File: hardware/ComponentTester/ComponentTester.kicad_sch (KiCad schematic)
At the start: 18 parts, among them J1 Conn_01x06_Socket, J2 AVR-ISP-6, J3 Conn_02x07_Counter_Clockwise, J4 GameBoy_GamePak_DMG-09, SW1 SW_Push, U1 ATmega328P-A, X1 16MHz

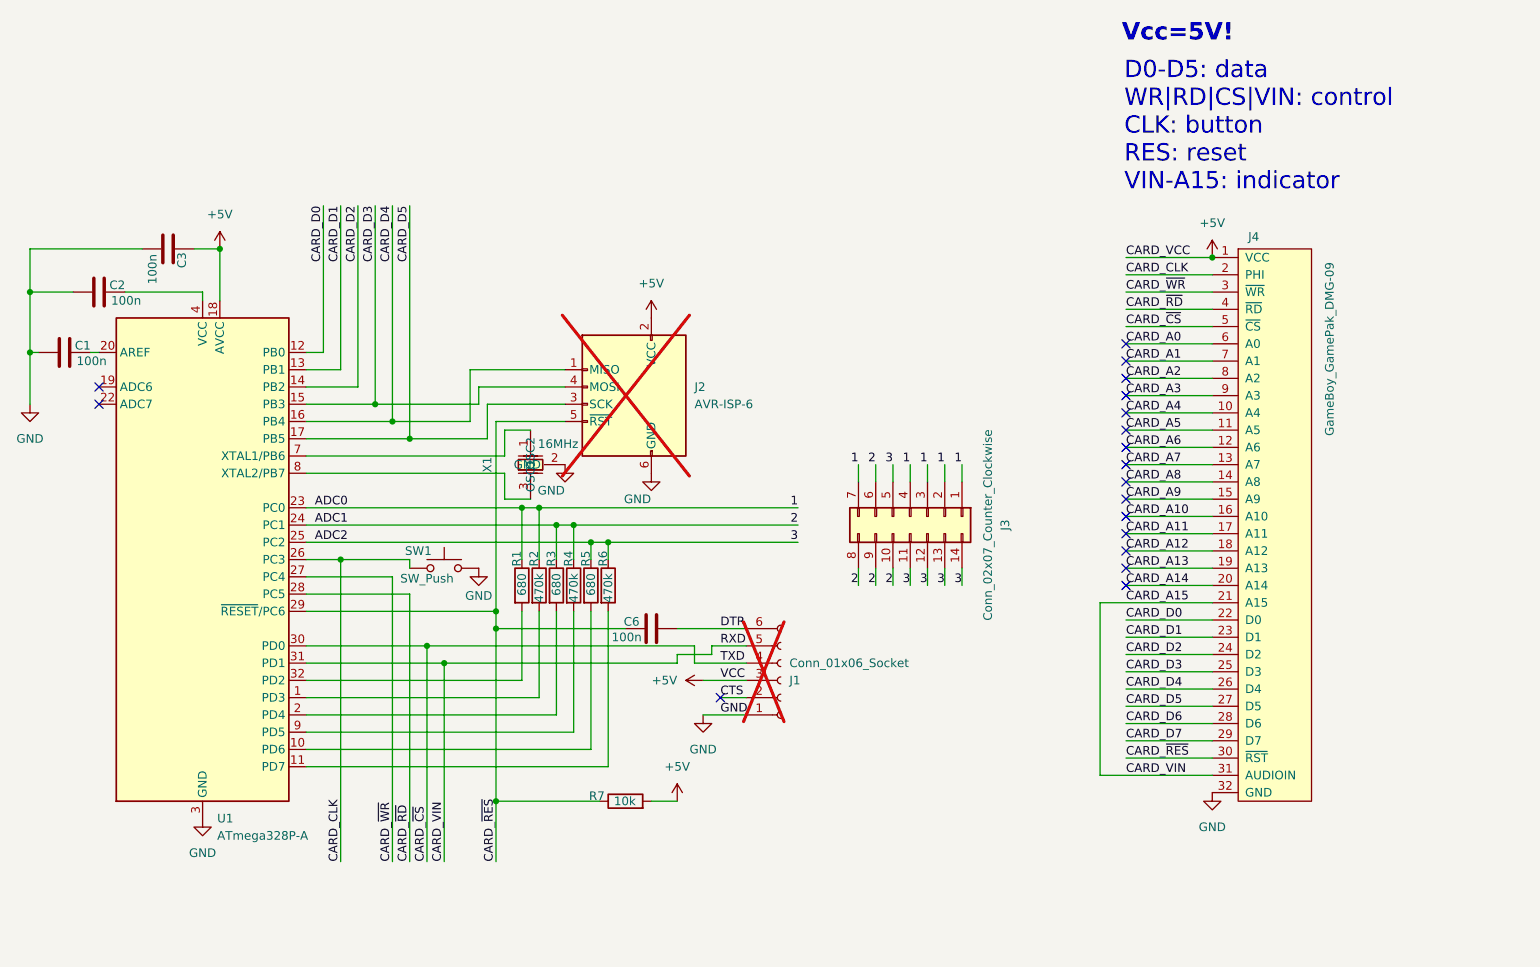
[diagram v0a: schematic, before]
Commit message: use ADC6 + ADC7
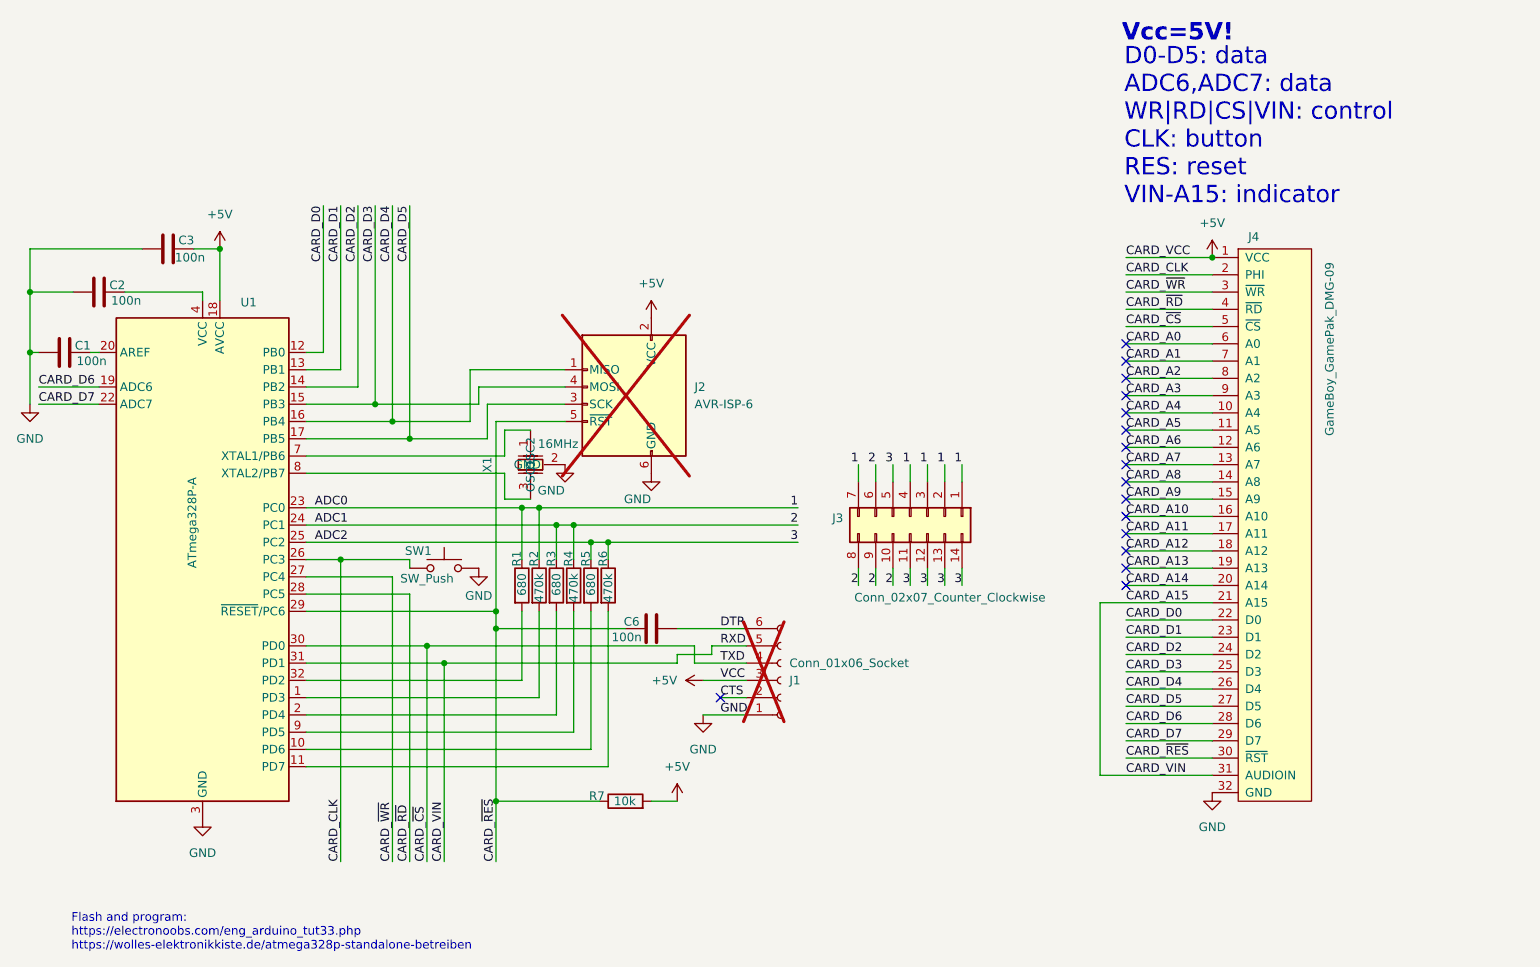
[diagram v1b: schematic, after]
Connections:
- net CARD_D6: now also U1.19 (ADC6)
- net CARD_D7: now also U1.22 (ADC7)
- no-connect marks 18 -> 16
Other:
- note added: "D0-D5: data ADC6,ADC7: data WR|RD|CS|VIN: control CLK: button RES: reset VIN-A15: indicator"
- note added: "Flash and program: https://electronoobs.com/eng_arduino_tut33.php https://wolles-elektronikkiste.de/atmega328p-standalone-betreiben"
- note removed: "D0-D5: data WR|RD|CS|VIN: control CLK: button RES: reset VIN-A15: indicator"
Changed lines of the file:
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@@
 	(generator_version "9.0")
 	(paper "A4")
+	(text "Flash and program:\nhttps://electronoobs.com/eng_arduino_tut33.php\nhttps://wolles-elektronikkiste.de/atmega328p-standalone-betreiben"
+		(exclude_from_sim no)
+		(at 54.356 166.624 0)
+		(effects
+			(font
+				(size 1.27 1.27)
+			)
+			(justify left)
+		)
+	)
 	(text "Vcc=5V!"
 		(exclude_from_sim no)
@@
 		)
 	)
-	(text "D0-D5: data\nWR|RD|CS|VIN: control\nCLK: button\nRES: reset\nVIN-A15: indicator"
+	(text "D0-D5: data\nADC6,ADC7: data\nWR|RD|CS|VIN: control\nCLK: button\nRES: reset\nVIN-A15: indicator"
 		(exclude_from_sim no)
 		(at 209.296 48.006 0)
@@
 	)
 	(no_connect
-		(at 58.42 88.9)
-	)
-	(no_connect
 		(at 209.55 80.01)
 	)
@@
 	)
 	(no_connect
-		(at 58.42 86.36)
-	)
-	(no_connect
 		(at 209.55 92.71)
 	)
@@
 	(wire
 		(pts
+			(xy 49.53 86.36) (xy 58.42 86.36)
+		)
+		(stroke
+			(width 0)
+			(type default)
+		)
+	)
+	(wire
+		(pts
 			(xy 120.65 104.14) (xy 123.19 104.14)
 		)
@@
 	(wire
 		(pts
+			(xy 49.53 88.9) (xy 58.42 88.9)
+		)
+		(stroke
+			(width 0)
+			(type default)
+		)
+	)
+	(wire
+		(pts
 			(xy 88.9 81.28) (xy 91.44 81.28)
 		)
@@
 		)
 	)
+	(label "CARD_D7"
+		(at 49.53 88.9 0)
+		(effects
+			(font
+				(size 1.27 1.27)
+			)
+			(justify left bottom)
+		)
+	)
 	(label "2"
 		(at 172.72 97.79 180)
@@
 		)
 	)
+	(label "CARD_D6"
+		(at 49.53 86.36 0)
+		(effects
+			(font
+				(size 1.27 1.27)
+			)
+			(justify left bottom)
+		)
+	)
 	(label "CARD_A9"
 		(at 209.55 102.87 0)
@@
 		(dnp no)
 		(property "Reference" "C3"
-			(at 70.612 66.548 0)
+			(at 70.104 64.77 90)
 			(effects
 				(font
@@
 		)
 		(property "Value" "100n"
-			(at 66.294 66.802 0)
+			(at 69.596 67.31 90)
 			(effects
 				(font
@@
 		(on_board yes)
 		(dnp no)
-		(fields_autoplaced yes)
 		(property "Reference" "U1"
-			(at 75.8033 149.86 0)
+			(at 79.248 73.914 0)
 			(effects
 				(font
@@
 		)
 		(property "Value" "ATmega328P-A"
-			(at 75.8033 152.4 0)
+			(at 72.136 113.03 90)
 			(effects
 				(font
@@
 			)
 		)
-		(property "Datasheet" "http://ww1.microchip.com/downloads/en/DeviceDoc/ATmega328_P%20AVR%20MCU%20with%20picoPower%20Technology%20Data%20Sheet%2040001984A.pdf"
+		(property "Datasheet" "https://ww1.microchip.com/downloads/aemDocuments/documents/MCU08/ProductDocuments/DataSheets/ATmega48A-PA-88A-PA-168A-PA-328-P-DS-DS40002061B.pdf"
 			(at 73.66 111.76 0)
 			(effects
@@
 		(on_board yes)
 		(dnp no)
-		(fields_autoplaced yes)
 		(property "Reference" "J3"
-			(at 191.77 106.68 0)
+			(at 167.132 105.664 90)
 			(effects
 				(font
@@
 		)
 		(property "Value" "Conn_02x07_Counter_Clockwise"
-			(at 189.23 106.68 0)
+			(at 183.642 117.348 90)
 			(effects
 				(font

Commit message: remove ext. crystal
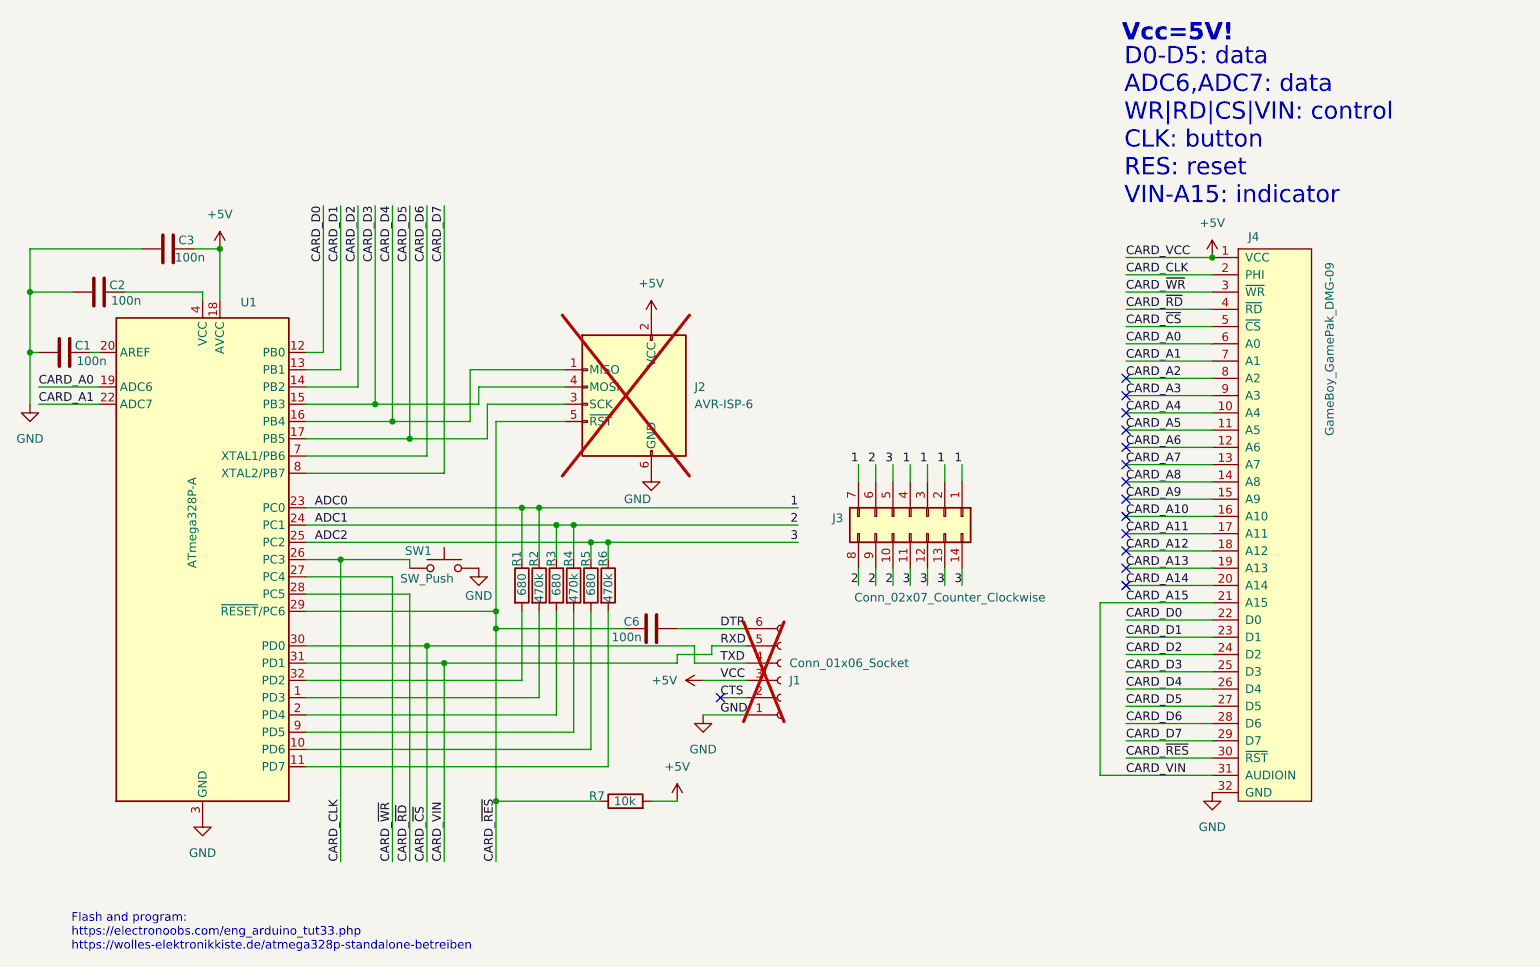
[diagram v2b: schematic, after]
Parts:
- removed X1: 16MHz, EasyEDA:OSC-SMD_3P-L3.2-W1.3-P1.2-L, symbol EasyEDA:CSTNE16M0V530000R0
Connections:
- net CARD_A0: now also U1.19 (ADC6)
- net CARD_A1: now also U1.22 (ADC7)
- net CARD_D6: now also U1.7 (XTAL1/PB6); no longer U1.19 (ADC6)
- net CARD_D7: now also U1.8 (XTAL2/PB7); no longer U1.22 (ADC7)
- no-connect marks 16 -> 14
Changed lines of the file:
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@@
 	)
 	(no_connect
-		(at 209.55 82.55)
-	)
-	(no_connect
 		(at 209.55 87.63)
 	)
@@
 	)
 	(no_connect
-		(at 209.55 80.01)
-	)
-	(no_connect
 		(at 149.86 132.08)
 	)
@@
 	(wire
 		(pts
-			(xy 114.3 88.9) (xy 99.06 88.9)
+			(xy 109.22 99.06) (xy 88.9 99.06)
 		)
 		(stroke
@@
 	(wire
 		(pts
-			(xy 148.59 125.73) (xy 143.51 125.73)
+			(xy 114.3 88.9) (xy 99.06 88.9)
 		)
 		(stroke
@@
 	(wire
 		(pts
-			(xy 106.68 124.46) (xy 106.68 156.21)
+			(xy 148.59 125.73) (xy 143.51 125.73)
 		)
 		(stroke
@@
 	(wire
 		(pts
-			(xy 182.88 97.79) (xy 182.88 100.33)
+			(xy 106.68 124.46) (xy 106.68 156.21)
 		)
 		(stroke
@@
 	(wire
 		(pts
-			(xy 96.52 59.69) (xy 96.52 86.36)
+			(xy 182.88 97.79) (xy 182.88 100.33)
 		)
 		(stroke
@@
 	(wire
 		(pts
-			(xy 118.11 96.52) (xy 88.9 96.52)
+			(xy 96.52 59.69) (xy 96.52 86.36)
 		)
 		(stroke
@@
 	(wire
 		(pts
-			(xy 118.11 99.06) (xy 88.9 99.06)
-		)
-		(stroke
-			(width 0)
-			(type default)
-		)
-	)
-	(wire
-		(pts
 			(xy 209.55 72.39) (xy 222.25 72.39)
 		)
@@
 	(wire
 		(pts
+			(xy 109.22 59.69) (xy 109.22 99.06)
+		)
+		(stroke
+			(width 0)
+			(type default)
+		)
+	)
+	(wire
+		(pts
 			(xy 48.26 81.28) (xy 48.26 72.39)
 		)
@@
 	(wire
 		(pts
-			(xy 118.11 92.71) (xy 118.11 96.52)
-		)
-		(stroke
-			(width 0)
-			(type default)
-		)
-	)
-	(wire
-		(pts
 			(xy 104.14 93.98) (xy 88.9 93.98)
 		)
@@
 	(wire
 		(pts
+			(xy 106.68 59.69) (xy 106.68 96.52)
+		)
+		(stroke
+			(width 0)
+			(type default)
+		)
+	)
+	(wire
+		(pts
 			(xy 49.53 88.9) (xy 58.42 88.9)
 		)
@@
 	(wire
 		(pts
-			(xy 121.92 92.71) (xy 118.11 92.71)
+			(xy 88.9 124.46) (xy 106.68 124.46)
 		)
 		(stroke
@@
 	(wire
 		(pts
-			(xy 88.9 124.46) (xy 106.68 124.46)
+			(xy 106.68 96.52) (xy 88.9 96.52)
 		)
 		(stroke
@@
 	(wire
 		(pts
-			(xy 118.11 99.06) (xy 118.11 102.87)
-		)
-		(stroke
-			(width 0)
-			(type default)
-		)
-	)
-	(wire
-		(pts
 			(xy 93.98 111.76) (xy 104.14 111.76)
 		)
@@
 	(wire
 		(pts
-			(xy 118.11 102.87) (xy 121.92 102.87)
-		)
-		(stroke
-			(width 0)
-			(type default)
-		)
-	)
-	(wire
-		(pts
 			(xy 123.19 132.08) (xy 88.9 132.08)
 		)
@@
 	)
 	(label "CARD_D7"
-		(at 49.53 88.9 0)
+		(at 109.22 59.69 270)
 		(effects
 			(font
 				(size 1.27 1.27)
 			)
-			(justify left bottom)
+			(justify right bottom)
 		)
 	)
@@
 		)
 	)
+	(label "CARD_A0"
+		(at 49.53 86.36 0)
+		(effects
+			(font
+				(size 1.27 1.27)
+			)
+			(justify left bottom)
+		)
+	)
 	(label "CARD_D0"
 		(at 91.44 59.69 270)
@@
 		)
 	)
+	(label "CARD_A1"
+		(at 49.53 88.9 0)
+		(effects
+			(font
+				(size 1.27 1.27)
+			)
+			(justify left bottom)
+		)
+	)
 	(label "2"
 		(at 170.18 115.57 180)
@@
 	)
 	(label "CARD_D6"
-		(at 49.53 86.36 0)
+		(at 106.68 59.69 270)
 		(effects
 			(font
 				(size 1.27 1.27)
 			)
-			(justify left bottom)
+			(justify right bottom)
 		)
 	)
@@
 	)
 	(symbol
-		(lib_id "EasyEDA:CSTNE16M0V530000R0")
-		(at 121.92 97.79 90)
-		(unit 1)
-		(exclude_from_sim no)
-		(in_bom yes)
-		(on_board yes)
-		(dnp no)
-		(property "Reference" "X1"
-			(at 115.57 97.79 0)
-			(effects
-				(font
-					(size 1.27 1.27)
-				)
-			)
-		)
-		(property "Value" "16MHz"
-			(at 125.984 94.742 90)
-			(effects
-				(font
-					(size 1.27 1.27)
-				)
-			)
-		)
-		(property "Footprint" "EasyEDA:OSC-SMD_3P-L3.2-W1.3-P1.2-L"
-			(at 134.62 97.79 0)
-			(effects
-				(font
-					(size 1.27 1.27)
-				)
-				(hide yes)
-			)
-		)
-		(property "Datasheet" "https://lcsc.com/product-detail/Others_Murata-Electronics-CSTNE16M0V530000R0_C341521.html"
-			(at 137.16 97.79 0)
-			(effects
-				(font
-					(size 1.27 1.27)
-				)
-				(hide yes)
-			)
-		)
-		(property "Description" ""
-			(at 121.92 97.79 0)
-			(effects
-				(font
-					(size 1.27 1.27)
-				)
-				(hide yes)
-			)
-		)
-		(property "LCSC Part" "C341521"
-			(at 139.7 97.79 0)
-			(effects
-				(font
-					(size 1.27 1.27)
-				)
-				(hide yes)
-			)
-		)
-		(pin "2"
-		)
-		(pin "3"
-		)
-		(pin "1"
-		)
-		(instances
-			(project ""
-				(path "/80bd7774-bbdd-4a53-bd07-874de5be49cb"
-					(reference "X1")
-					(unit 1)
-				)
-			)
-		)
-	)
-	(symbol
 		(lib_id "power:GND")
 		(at 48.26 88.9 0)
@@
 					(unit 1)
 				)
-			)
-		)
-	)
-	(symbol
-		(lib_id "power:GND")
-		(at 127 97.79 0)
-		(unit 1)
-		(exclude_from_sim no)
-		(in_bom yes)
-		(on_board yes)
-		(dnp no)
-		(property "Reference" "#PWR012"
-			(at 127 104.14 0)
-			(effects
-				(font
-					(size 1.27 1.27)
-				)
-				(hide yes)
-			)
-		)
-		(property "Value" "GND"
-			(at 124.968 101.6 0)
-			(effects
-				(font
-					(size 1.27 1.27)
-				)
-			)
-		)
-		(property "Footprint" ""
-			(at 127 97.79 0)
-			(effects
-				(font
-					(size 1.27 1.27)
-				)
-				(hide yes)
-			)
-		)
-		(property "Datasheet" ""
-			(at 127 97.79 0)
-			(effects
-				(font
-					(size 1.27 1.27)
-				)
-				(hide yes)
-			)
-		)
-		(property "Description" "Power symbol creates a global label with name \"GND\" , ground"
-			(at 127 97.79 0)
-			(effects
-				(font
-					(size 1.27 1.27)
-				)
-				(hide yes)
-			)
-		)
-		(pin "1"
-		)
-		(instances
-			(project "ComponentTester"
-				(path "/80bd7774-bbdd-4a53-bd07-874de5be49cb"
-					(reference "#PWR012")
-					(unit 1)
-				)

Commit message: clean up
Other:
- note added: "D0-D7: data ADC6,ADC7: data WR|RD|CS|VIN: control CLK: button RES: reset <-> pull low VIN-A15: indicator"
- note removed: "D0-D5: data ADC6,ADC7: data WR|RD|CS|VIN: control CLK: button RES: reset VIN-A15: indicator"
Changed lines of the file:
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@@
 		)
 	)
-	(text "D0-D5: data\nADC6,ADC7: data\nWR|RD|CS|VIN: control\nCLK: button\nRES: reset\nVIN-A15: indicator"
+	(text "D0-D7: data\nADC6,ADC7: data\nWR|RD|CS|VIN: control\nCLK: button\nRES: reset <-> pull low\nVIN-A15: indicator"
 		(exclude_from_sim no)
 		(at 209.296 48.006 0)
@@
 		(on_board yes)
 		(dnp no)
-		(fields_autoplaced yes)
 		(property "Reference" "#PWR08"
 			(at 151.13 129.54 0)
